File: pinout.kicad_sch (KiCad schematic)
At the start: 1 part

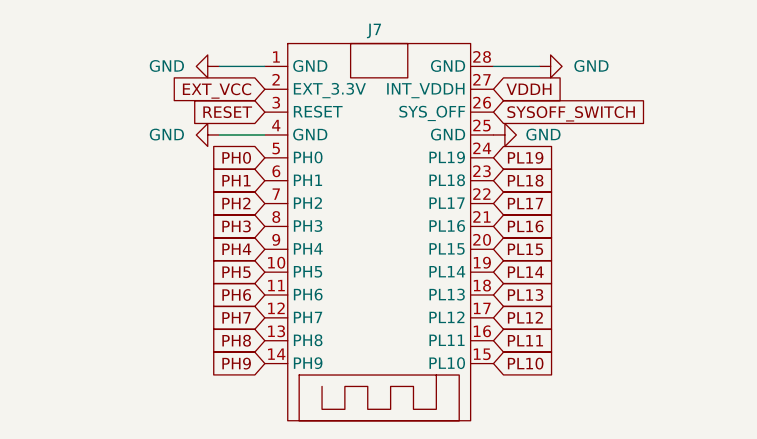
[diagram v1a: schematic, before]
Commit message: Routing Done; DFM problems to solve
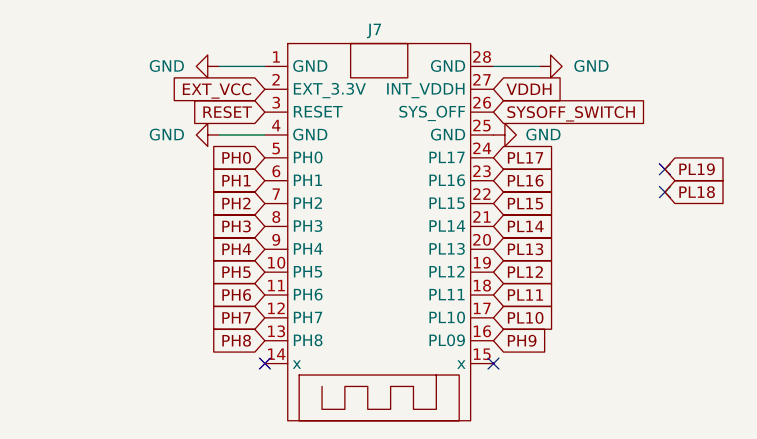
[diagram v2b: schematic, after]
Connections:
- net PH9: now also J7.16 (PL09); no longer J7.14 (PH9)
- net PL10: now also J7.17 (PL10); no longer J7.15 (PL10)
- net PL11: now also J7.18 (PL11); no longer J7.16 (PL11)
- net PL12: now also J7.19 (PL12); no longer J7.17 (PL12)
- net PL13: now also J7.20 (PL13); no longer J7.18 (PL13)
- net PL14: now also J7.21 (PL14); no longer J7.19 (PL14)
- net PL15: now also J7.22 (PL15); no longer J7.20 (PL15)
- net PL16: now also J7.23 (PL16); no longer J7.21 (PL16)
- net PL17: now also J7.24 (PL17); no longer J7.22 (PL17)
- net PL18: no longer J7.23 (PL18)
- net PL19: no longer J7.24 (PL19)
- no-connect marks 0 -> 4

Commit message: Replaced IC with NINA Module
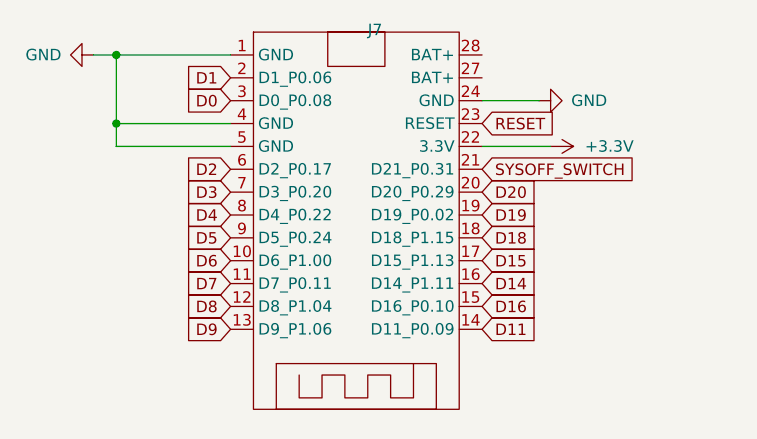
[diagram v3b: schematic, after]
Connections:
- net PH0 is gone; now on net GND: J7.5 (GND)
- net PL14 is gone; now on net SYSOFF_SWITCH: J7.21 (D21_P0.31)
- net PL16 is gone; now on net RESET: J7.23 (RESET)
- net PL17 is gone; now on net GND: J7.24 (GND)
- net GND: no longer J7.25 (GND), J7.28 (GND)
- net RESET: no longer J7.3 (RESET)
- net SYSOFF_SWITCH: no longer J7.26 (SYS_OFF)
- net D11: now reaches J7.14 (D11_P0.09)
- net D16: now reaches J7.15 (D16_P0.10)
- net EXT_VCC renamed D1
- net PH1 renamed D2
- net PH2 renamed D3
- net PH3 renamed D4
- net PH4 renamed D5
- net PH5 renamed D6
- net PH6 renamed D7
- net PH7 renamed D8
- net PH8 renamed D9
- net PH9 renamed D14
- net PL10 renamed D15
- net PL11 renamed D18
- net PL12 renamed D19
- net PL13 renamed D20
- net PL15 renamed +3.3V
- net VDDH: no longer names the net of J7.27 (BAT+)
- new net D0: J7.3 (D0_P0.08)
- no-connect marks 4 -> 0
